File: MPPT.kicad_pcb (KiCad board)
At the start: 2 copper layers, 125 x 145 mm, 135 parts, among them J1 Car Power, J2 9V Supply, J3 Solar Array, J4 Battery, J5 CAN_In, J6 CAN_Out, Q1 NMOS, Q2 NMOS, SW1 SW_Push, SW2 SW_DIP_x02, U1 RI3-1205S, U10 CDSOT23-T24CAN, U2 MCU_Nucleo_L432KC, U3 UCC37321, U4 IES01_PDS1, U5 INA210, U6 INA210, U7 MAX40075, U8 MAX40075, U9 ADM3055E

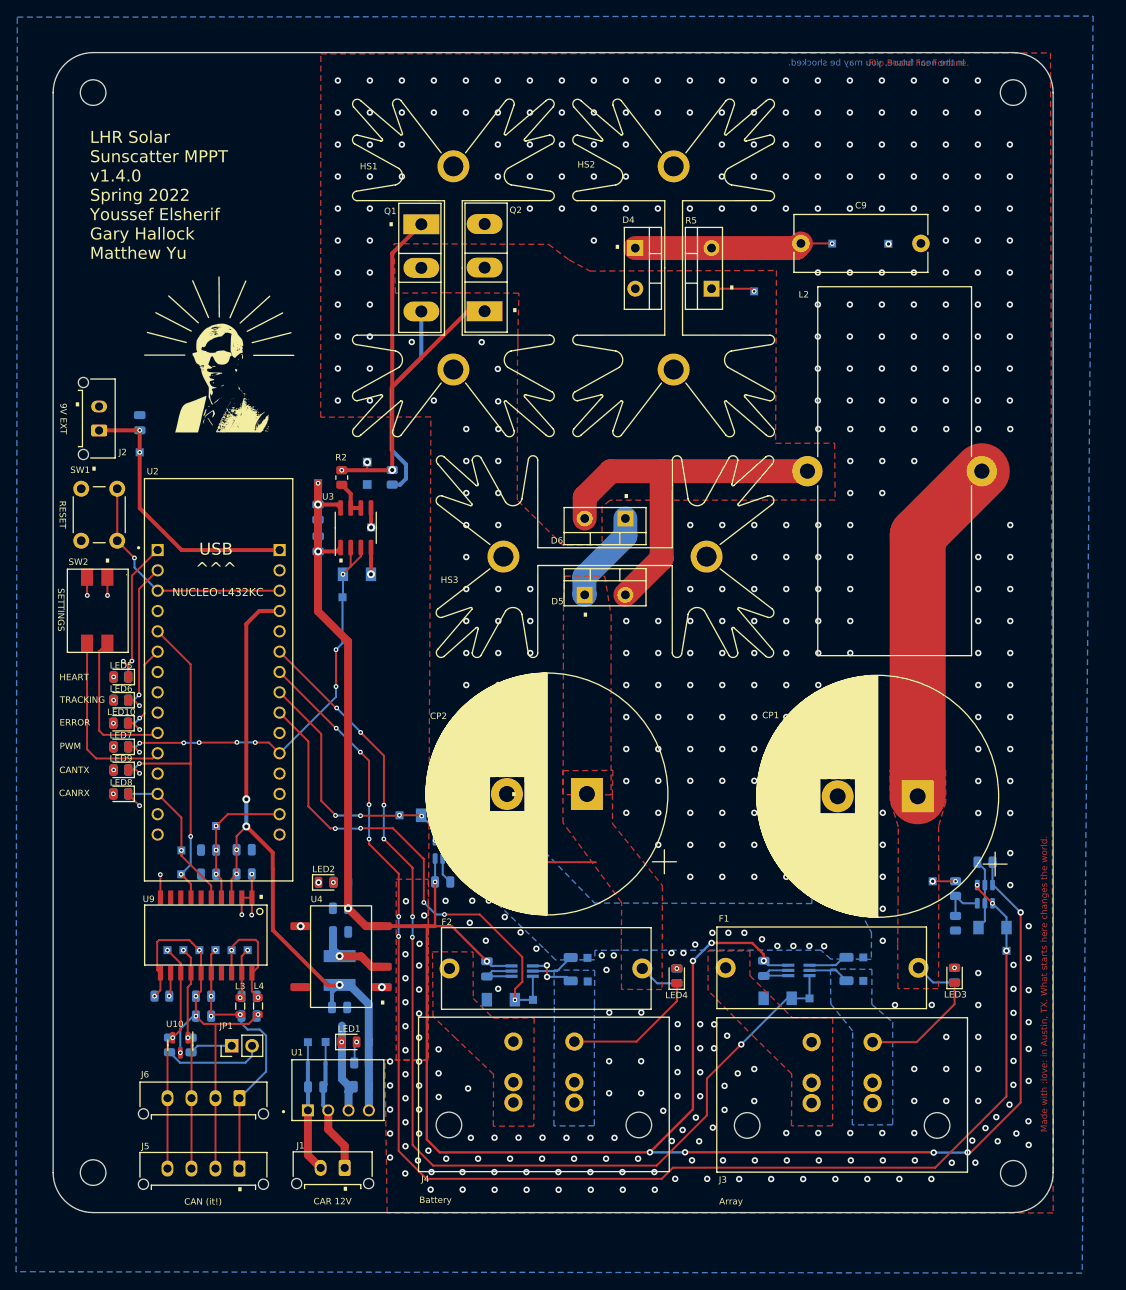
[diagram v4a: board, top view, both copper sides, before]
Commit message: gerber rebuild for JLPCB errors
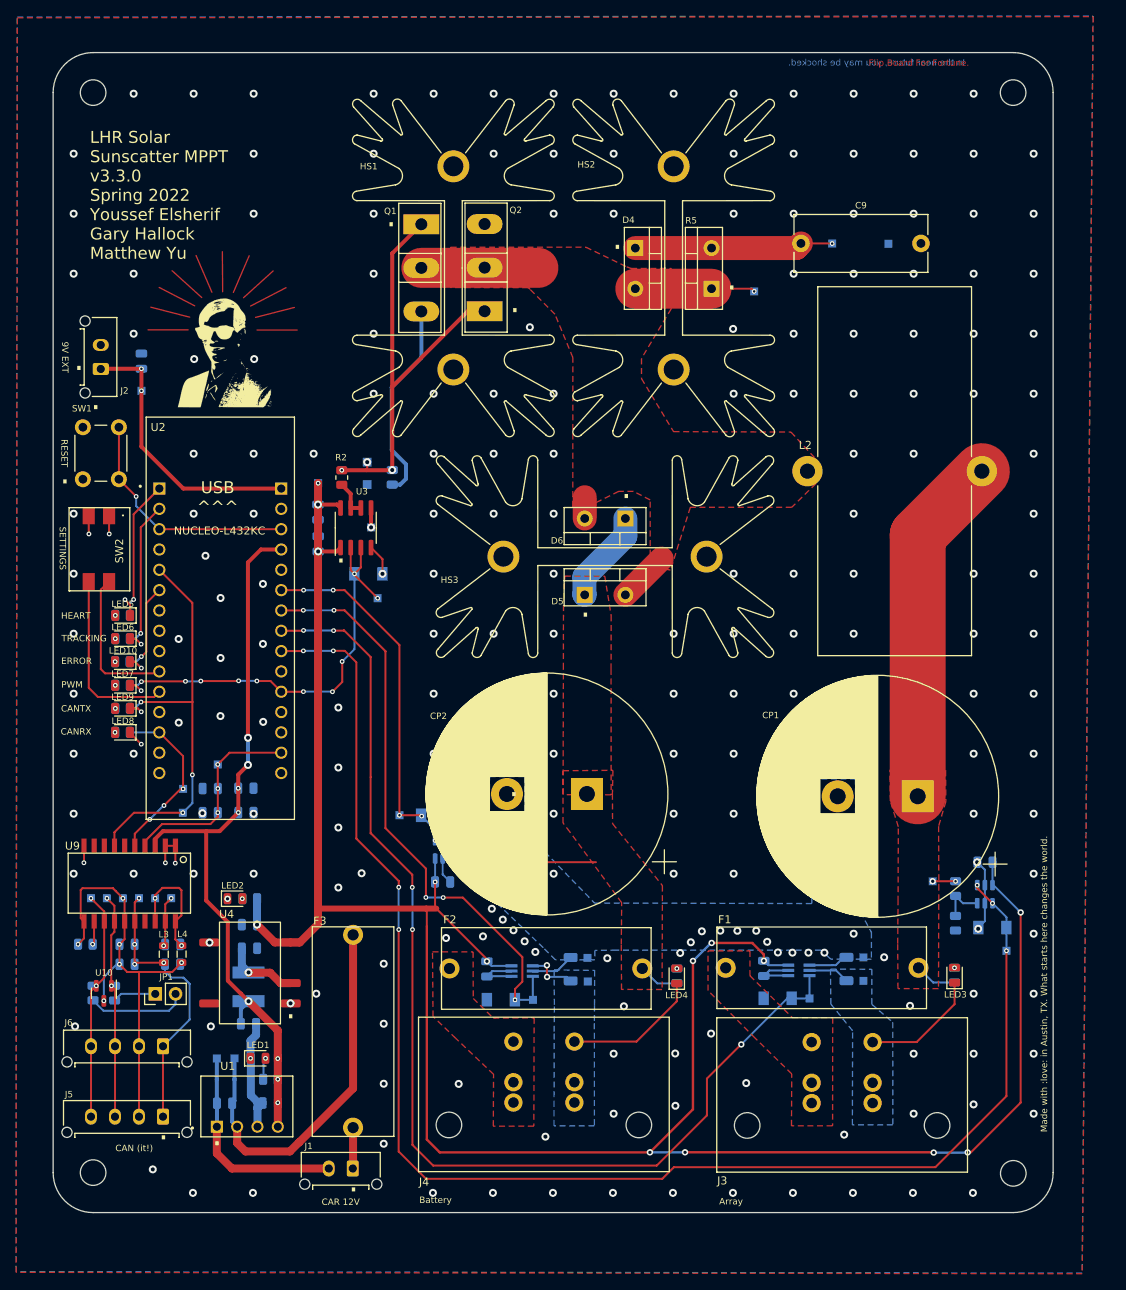
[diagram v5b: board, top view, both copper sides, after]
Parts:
- removed REF**: ESD-Logo_8.9x8mm_SilkScreen, Symbol:ESD-Logo_8.9x8mm_SilkScreen
- removed REF**: KiCad-Logo2_5mm_SilkScreen, Symbol:KiCad-Logo2_5mm_SilkScreen
- added F3: Fuse, Footprints:05200101Z_Fuze_Holder_5x20_PCB_Mount, F.Cu at (60.1, 126.8)
- F1, F2: footprint MPPT:05200101Z_Fuze_Holder_5x20_PCB_Mount -> Footprints:05200101Z_Fuze_Holder_5x20_PCB_Mount
- J3, J4: footprint MPPT:PhoenixContact_PowerCombicon5_GF_2x7.62mm -> Footprints:PhoenixContact_PowerCombicon5_GF_2x7.62mm
- L2: footprint MPPT:L_Toroid_Vertical_L46.0mm_W19.1mm_P21.80mm_Bourns_5700 -> Footprints:L_Toroid_Vertical_L46.0mm_W19.1mm_P21.80mm_Bourns_5700
- SW2: footprint MPPT:ADF02ST04_DIP_Switch_2_POS -> Footprints:ADF02ST04_DIP_Switch_2_POS
- U1: footprint MPPT:CONV_RI3-1205S -> Footprints:CONV_RI3-1205S
- U2: footprint MPPT:MODULE_NUCLEO-L432KC -> Footprints:MODULE_NUCLEO-L432KC
- U4: footprint MPPT:IES01_PDS1 -> Footprints:IES01_PDS1
- U9: footprint MPPT:ADM3055EBRIZ -> Footprints:ADM3055EBRIZ
- moved C2 11.6 mm to (44.6, 148.8)
- moved C8 11.6 mm to (42.0, 126.5)
- moved L1 11.6 mm to (41.9, 134.3)
- moved LED1 11.6 mm to (43.1, 143.2)
- moved R1 11.6 mm to (44.7, 145.8)
- moved TP6 11.6 mm to (42.2, 143.2)
- moved C1 11.6 mm to (38.9, 148.8)
- moved D1 11.6 mm to (39.1, 145.8)
- moved TP2 11.6 mm to (38.0, 143.2)
- moved U1 11.6 mm to (41.7, 149.2)
- moved U4 11.6 mm to (45.9, 138.9)
- moved C7 11.6 mm to (42.0, 129.4)
- moved LED2 11.6 mm to (40.2, 123.2)
- moved R3 11.6 mm to (42.1, 123.2)
- moved C6 11.6 mm to (41.9, 138.9)
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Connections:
- J1 pad 1: +12V -> Net-(F3-Pad2)
- U2 pad 22: /Battery_Current -> /Array_Voltage
- U2 pad 23: /Battery_Voltage -> /Array_Current
- U2 pad 24: /Array_Voltage -> /Battery_Current
- U2 pad 25: /Array_Current -> /Battery_Voltage
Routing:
- net +12V: track 17.0 -> 48.4 mm
- net Net-(D4-Pad2): track 54.7 -> 38.7 mm
- net +9VA: track 272.2 -> 286.0 mm
- net /Battery_Voltage: track 36.0 -> 48.5 mm
- net /Battery_Current: track 61.9 -> 74.1 mm
- net GNDPWR: track 16.3 -> 26.6 mm
- net +5V: track 84.8 -> 93.1 mm, vias 5 -> 8
- net /CAN_Tx: track 44.1 -> 52.0 mm
- net +3V3: track 17.7 -> 25.5 mm
- net /Array_Current: track 133.5 -> 140.7 mm, vias 7 -> 5
- net /Array_Voltage: track 175.8 -> 182.9 mm, vias 9 -> 7
- net Net-(F3-Pad2): track 0.00 -> 5.07 mm
- net /CAN_Rx: track 19.4 -> 21.8 mm, vias 1 -> 3
- net /PWM: track 51.6 -> 53.0 mm, vias 8 -> 10
- net GND: track 110.5 -> 109.9 mm, vias 492 -> 241
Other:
- board text added: "Hey, we've been trying to reach you concerning your vehicle's extended warranty..."
- board text added: "LHR Solar Sunscatter MPPT v3.3.0 Spring 2022 Youssef Elsherif Gary Hallock Matthew Yu"
- board text removed: "Hey, we've trying to reach you concerning your vehicle's extended warranty..."
- board text removed: "LHR Solar Sunscatter MPPT v1.4.0 Spring 2022 Youssef Elsherif Gary Hallock Matthew Yu"
